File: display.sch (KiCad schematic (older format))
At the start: 23 parts, among them P1 USB, P10 NAV_TRANS, P11 NAV_ID, P12 NAV_VOL, P2 Power, P3 SPI Debug, P4 LED_JUMPER, P5 COM_ENC, P6 COM_STEP, P7 COM_TRANS, P8 COM_VOL, P9 NAV_ENC, U1 ATmega32U4, U10 RESET

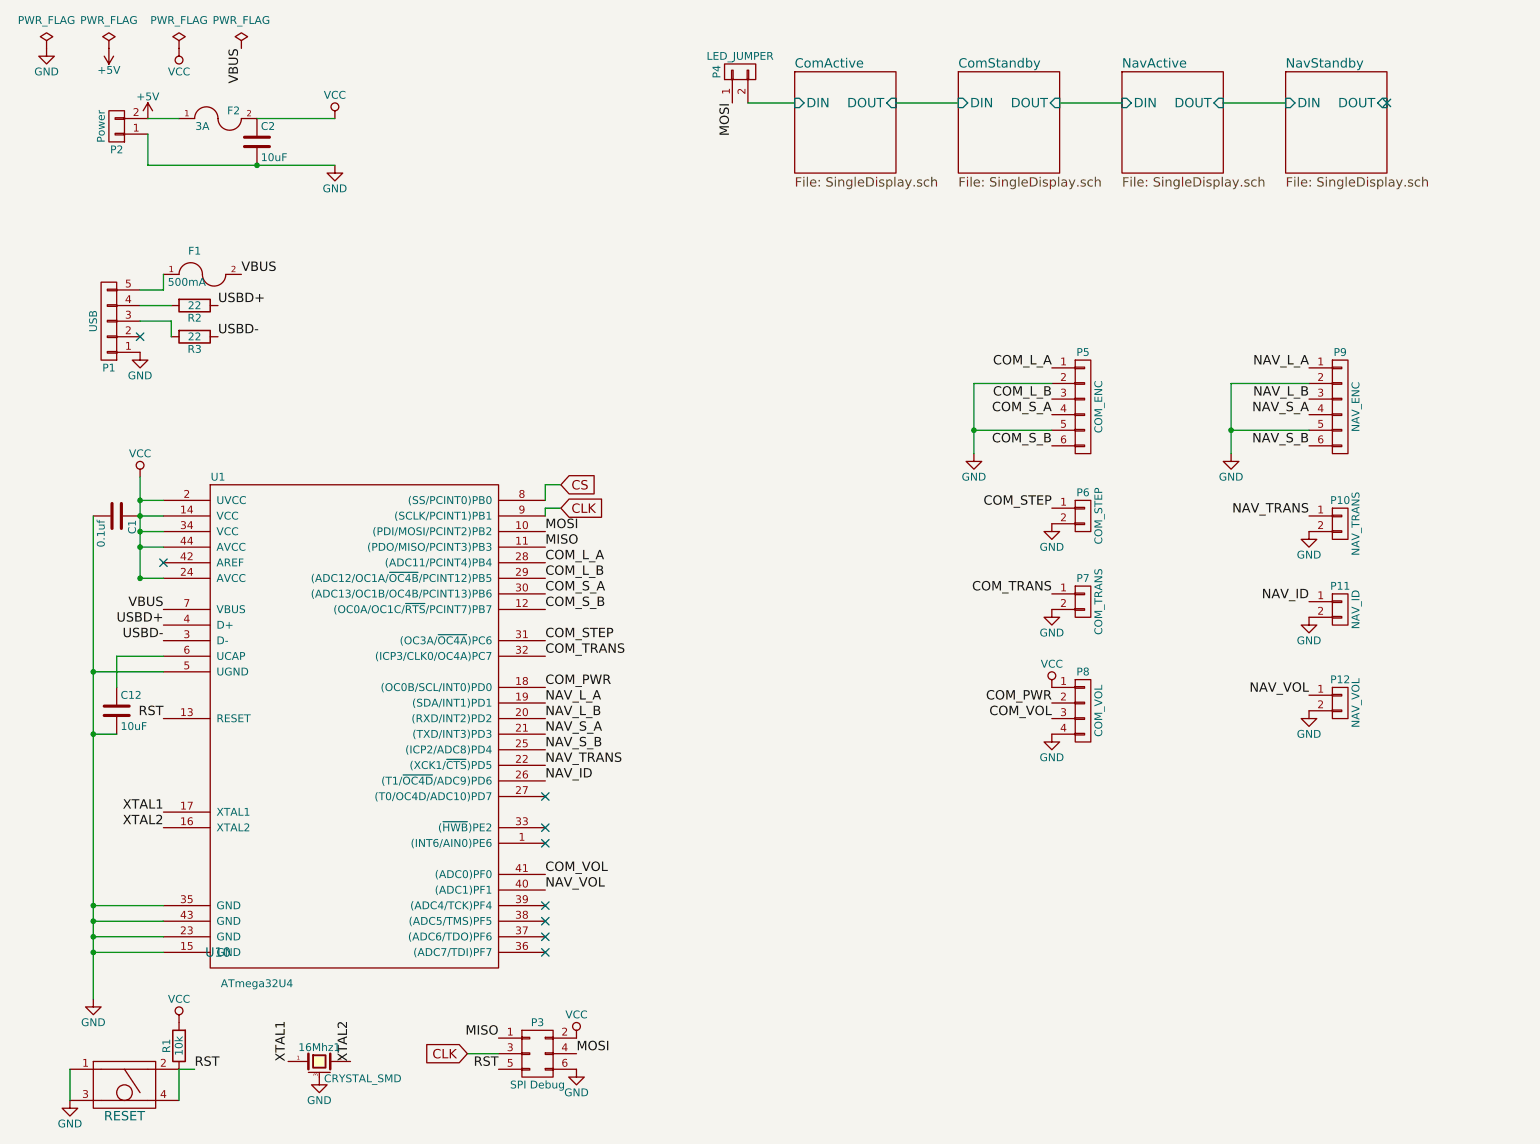
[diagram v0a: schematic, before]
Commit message: Finished trace routing.  Added 3d parts
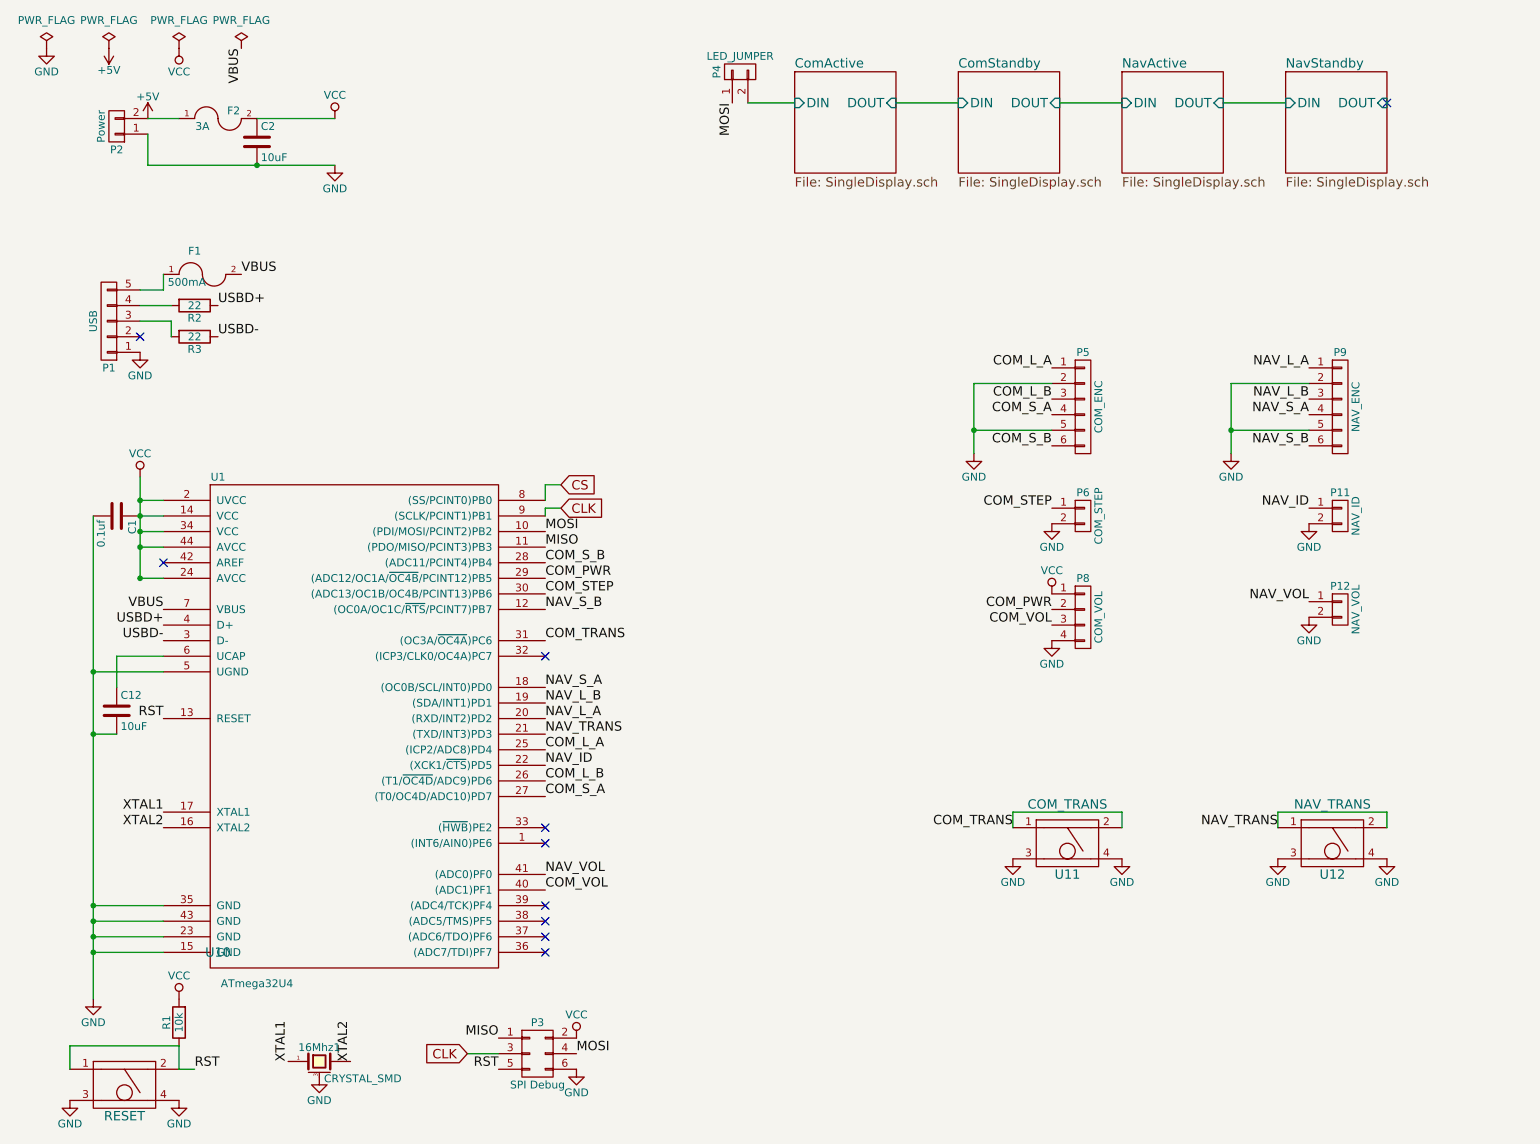
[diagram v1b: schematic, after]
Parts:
- removed P10: NAV_TRANS, custom:JST-ZH-THRx2, symbol CONN_01X02
- removed P7: COM_TRANS, custom:JST-ZH-THRx2, symbol CONN_01X02
- added U11: COM_TRANS, custom:TAC_SWITCH_CK_KSC4_JWING, symbol TAC_SWITCH_PTS645
- added U12: NAV_TRANS, custom:TAC_SWITCH_CK_KSC4_JWING, symbol TAC_SWITCH_PTS645
- P2, P4: footprint Pin_Headers:Pin_Header_Straight_1x02_Pitch2.54mm -> custom:Pin_Header_Straight_1x02_Pitch2.54mm
- P3: footprint Pin_Headers:Pin_Header_Straight_2x03_Pitch2.54mm -> custom:Pin_Header_Straight_2x03_Pitch2.54mm
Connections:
- net COM_L_A: now also U1.25 ((ICP2/ADC8)PD4); no longer U1.28 ((ADC11/PCINT4)PB4)
- net COM_L_B: now also U1.26 ((T1/~OC4D~/ADC9)PD6); no longer U1.29 ((ADC12/OC1A/~OC4B~/PCINT12)PB5)
- net COM_PWR: now also U1.29 ((ADC12/OC1A/~OC4B~/PCINT12)PB5); no longer U1.18 ((OC0B/SCL/INT0)PD0)
- net COM_STEP: now also U1.30 ((ADC13/OC1B/OC4B/PCINT13)PB6); no longer U1.31 ((OC3A/~OC4A~)PC6)
- net COM_S_A: now also U1.27 ((T0/OC4D/ADC10)PD7); no longer U1.30 ((ADC13/OC1B/OC4B/PCINT13)PB6)
- net COM_S_B: now also U1.28 ((ADC11/PCINT4)PB4); no longer U1.12 ((OC0A/OC1C/~RTS~/PCINT7)PB7)
- net COM_TRANS: now also U1.31 ((OC3A/~OC4A~)PC6), U11.1, U11.2; no longer U1.32 ((ICP3/CLK0/OC4A)PC7)
- net COM_VOL: now also U1.40 ((ADC1)PF1); no longer U1.41 ((ADC0)PF0)
- net GND: now also U10.4, U11.3, U11.4, U12.3, U12.4; no longer U10.1
- net NAV_ID: now also U1.22 ((XCK1/~CTS~)PD5); no longer U1.26 ((T1/~OC4D~/ADC9)PD6)
- net NAV_L_A: now also U1.20 ((RXD/INT2)PD2); no longer U1.19 ((SDA/INT1)PD1)
- net NAV_L_B: now also U1.19 ((SDA/INT1)PD1); no longer U1.20 ((RXD/INT2)PD2)
- net NAV_S_A: now also U1.18 ((OC0B/SCL/INT0)PD0); no longer U1.21 ((TXD/INT3)PD3)
- net NAV_S_B: now also U1.12 ((OC0A/OC1C/~RTS~/PCINT7)PB7); no longer U1.25 ((ICP2/ADC8)PD4)
- net NAV_TRANS: now also U1.21 ((TXD/INT3)PD3), U12.1, U12.2; no longer U1.22 ((XCK1/~CTS~)PD5)
- net NAV_VOL: now also U1.41 ((ADC0)PF0); no longer U1.40 ((ADC1)PF1)
- net RST: now also U10.1; no longer U10.4
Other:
- moved on the sheet: P11, P12, P8, R1

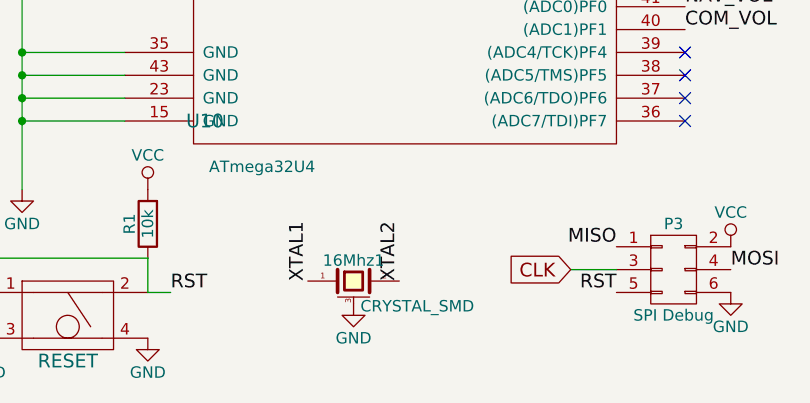
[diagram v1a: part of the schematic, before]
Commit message: Updated with actual dimensions from 7 segment displays.  Deleted unused files.
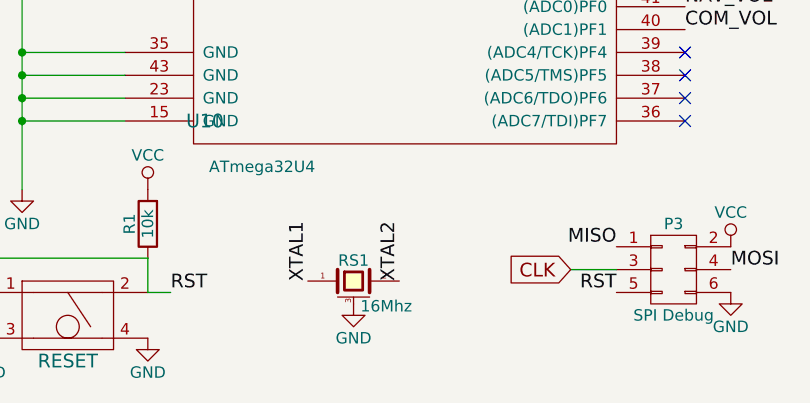
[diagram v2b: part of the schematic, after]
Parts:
- RS1: renamed from 16Mhz1; value CRYSTAL_SMD -> 16Mhz; footprint custom:Oscilator_Cap_SMD -> custom:RESONATOR_SMD_Abracon_AWSCR
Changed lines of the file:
@@
 NAV_ID
 $Comp
-L CRYSTAL_SMD 16Mhz1
+L CRYSTAL_SMD RS1
 U 1 1 59D66454
 P 2400 7250
-F 0 "16Mhz1" H 2400 7340 50  0000 C CNN
-F 1 "CRYSTAL_SMD" H 2430 7140 50  0000 L CNN
-F 2 "custom:Oscilator_Cap_SMD" H 2400 7250 50  0001 C CNN
+F 0 "RS1" H 2400 7340 50  0000 C CNN
+F 1 "16Mhz" H 2430 7140 50  0000 L CNN
+F 2 "custom:RESONATOR_SMD_Abracon_AWSCR" H 2400 7250 50  0001 C CNN
 F 3 "" H 2400 7250 50  0000 C CNN
 	1    2400 7250

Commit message: Tons of updates.  Mostly working.
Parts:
- added P7: LDR, custom:JST-ZH-THRx2, symbol CONN_01X02
- added R8: 10k, Resistors_SMD:R_0805, symbol R
- U1: symbol ATmega32U4 -> ATmega32U4-RESCUE-display
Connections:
- net GND: now also P7.2 (P2)
- net VCC: now also R8.1
- net LDR: now reaches U1.39 ((ADC4/TCK)PF4)
- net LDR: now also P7.1 (P1), R8.2
- no-connect marks 10 -> 9
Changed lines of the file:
@@
 EESchema Schematic File Version 2
+LIBS:display-rescue
 LIBS:power
 LIBS:device
@@
 $EndComp
 $Comp
-L ATmega32U4 U1
+L ATmega32U4-RESCUE-display U1
 U 1 1 59D3BE6F
 P 2650 5200
@@
 NoConn ~ 3850 5750
 NoConn ~ 3850 5850
-NoConn ~ 3850 6250
 NoConn ~ 3850 6350
 NoConn ~ 3850 6450
@@
 	1    0    0    -1
 $EndComp
+$Comp
+L CONN_01X02 P7
+U 1 1 59F2D087
+P 10000 4200
+F 0 "P7" H 10000 4350 50  0000 C CNN
+F 1 "LDR" V 10100 4200 50  0000 C CNN
+F 2 "custom:JST-ZH-THRx2" H 10000 4200 50  0001 C CNN
+F 3 "" H 10000 4200 50  0000 C CNN
+	1    10000 4200
+	1    0    0    -1
+$EndComp
+$Comp
+L R R8
+U 1 1 59F2D228
+P 9800 4000
+F 0 "R8" V 9880 4000 50  0000 C CNN
+F 1 "10k" V 9800 4000 50  0000 C CNN
+F 2 "Resistors_SMD:R_0805" V 9730 4000 50  0001 C CNN
+F 3 "" H 9800 4000 50  0000 C CNN
+	1    9800 4000
+	1    0    0    -1
+$EndComp
+$Comp
+L GND #PWR031
+U 1 1 59F2D30A
+P 9800 4250
+F 0 "#PWR031" H 9800 4000 50  0001 C CNN
+F 1 "GND" H 9800 4100 50  0000 C CNN
+F 2 "" H 9800 4250 50  0000 C CNN
+F 3 "" H 9800 4250 50  0000 C CNN
+	1    9800 4250
+	1    0    0    -1
+$EndComp
+Text Label 9700 4150 2    60   ~ 0
+LDR
+$Comp
+L VCC #PWR032
+U 1 1 59F2D47E
+P 9800 3850
+F 0 "#PWR032" H 9800 3700 50  0001 C CNN
+F 1 "VCC" H 9800 4000 50  0000 C CNN
+F 2 "" H 9800 3850 50  0000 C CNN
+F 3 "" H 9800 3850 50  0000 C CNN
+	1    9800 3850
+	1    0    0    -1
+$EndComp
+Text Label 3850 6250 0    60   ~ 0
+LDR
+Wire Wire Line
+	9700 4150 9800 4150
 $EndSCHEMATC
